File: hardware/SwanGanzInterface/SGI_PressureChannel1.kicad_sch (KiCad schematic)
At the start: 0 parts

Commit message: Developed amplifier circuits
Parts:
- added C10: 0.1u, Capacitor_SMD:C_0603_1608Metric, symbol Device:C
- added C11, C12: C, symbol Device:C
- added C13: 0.1u, symbol Device:C
- added R10, R11, R12: R, symbol Device:R
- added R13, R14: 0R, symbol Device:R
- added U4: INA122D, Package_SO:SOIC-8_5.3x5.3mm_P1.27mm, symbol SGI_SymbolLib:INA122D
- added U5: OPA2350, Package_DIP:DIP-8_W7.62mm, symbol SGI_SymbolLib:OPA2350PA
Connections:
- new net: R13.2, R14.1, U5.2 (-)
- new net: C11.1, R11.2, R12.1
- new net: C12.1, R12.2, U5.3 (+)
- new net: R10.1, U4.1 (RG+)
- new net: R11.1, U4.6 (OUT)
- new net: R10.2, U4.8 (RG-)
- new net +3V3A: C10.2, C13.1, U4.7 (+VS), U5.8 (V+)
- new net AGND: C10.1, C11.2, C13.2, R13.1, U4.4 (-VS), U4.5 (REF), U5.4 (V-)
- new net Pres1AmpOut: C12.2, R14.2, U5.1

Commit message: Filter Parameters
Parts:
- C11, C12: value C -> 0.1u
- R11, R12: value R -> 32k
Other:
- note added: "49.736 Hz Cutoff"
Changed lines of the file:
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@@
 	(generator "eeschema")
 	(generator_version "9.0")
-	(paper "A3")
+	(paper "A4")
 	(title_block
 		(title "Swan Ganz Interface")
-		(date "2025-12-20")
+		(date "2026-01-12")
 		(rev "Rev 1.0")
 		(company "Univerisity of Texas at Austin")
@@
 		(comment 2 "Ashton Knecht, Jack Son, Nathan DeLaRosa, Jerry Xia")
 		(comment 3 "Faculty Mentor - Dr. Valvano")
+	)
+	(text "49.736 Hz Cutoff"
+		(exclude_from_sim no)
+		(at 83.185 97.79 0)
+		(effects
+			(font
+				(size 2.54 2.54)
+			)
+		)
 	)
 	(junction
@@
 			)
 		)
-		(property "Value" "C"
+		(property "Value" "0.1u"
 			(at 105.41 71.755 0)
 			(effects
@@
 			)
 		)
-		(property "Value" "R"
+		(property "Value" "32k"
 			(at 111.76 62.23 90)
 			(effects
@@
 			)
 		)
-		(property "Value" "R"
+		(property "Value" "32k"
 			(at 97.79 62.23 90)
 			(effects
@@
 			)
 		)
-		(property "Value" "C"
-			(at 131.445 57.15 90)
-			(effects
-				(font
+		(property "Value" "0.1u"
+			(at 132.715 57.15 90)
+			(effects
+				(font

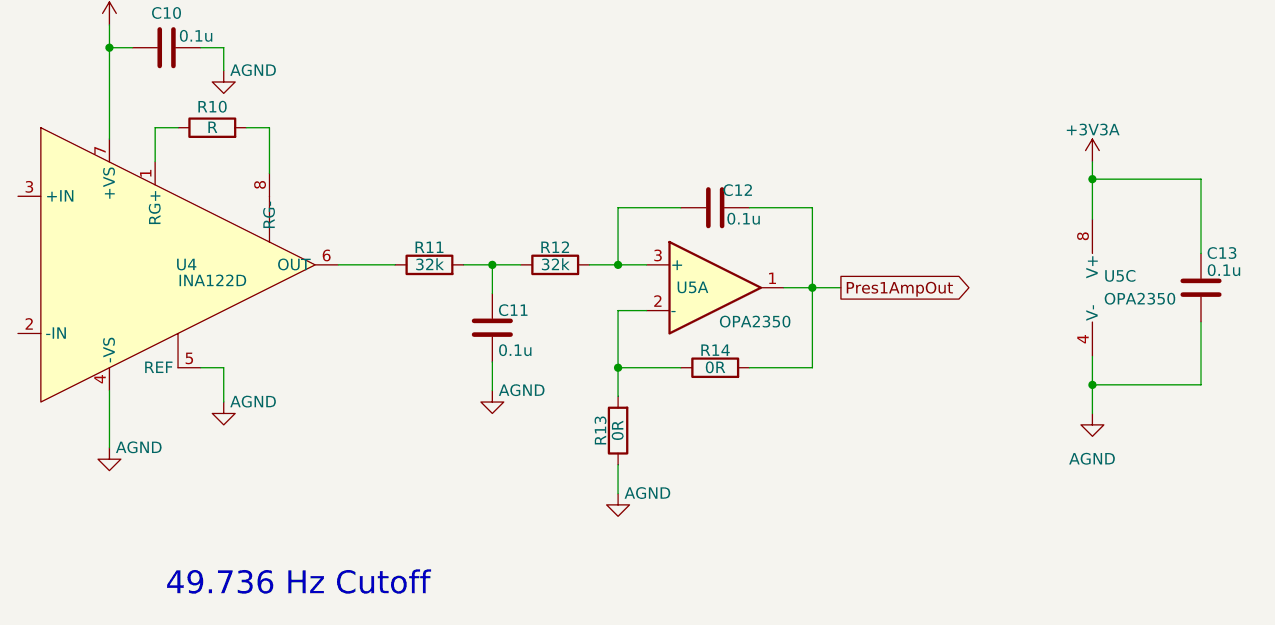
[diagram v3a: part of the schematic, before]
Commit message: Finished MSP-LP Symbol, Started Pressure_Connector Symbol
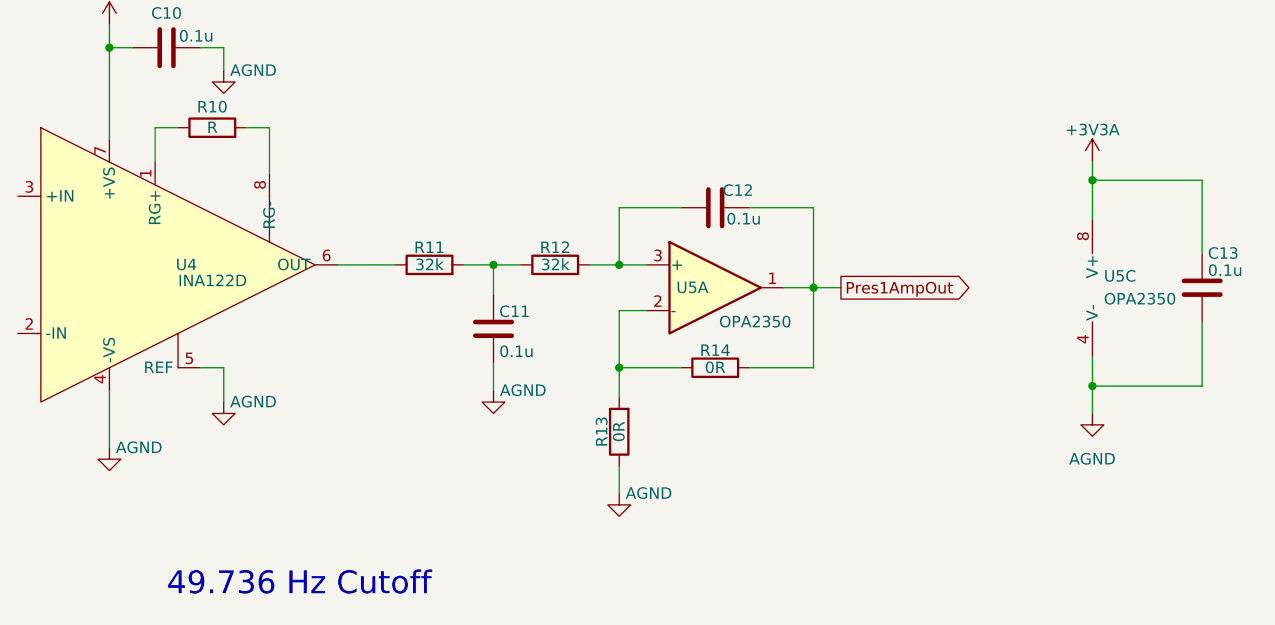
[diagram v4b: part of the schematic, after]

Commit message: Pressure Connector - Syncing for development
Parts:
- added U8: ~, symbol SGI_SymbolLib:Pressure_Connector
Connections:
- net AGND: now also U8.4 (VDD)
- net at U4.2 (-IN): now also U8.3 (SIG-)
- net at U4.3 (+IN): now also U8.2 (SIG+)
- new net P1_VCC: U8.1 (VCC)

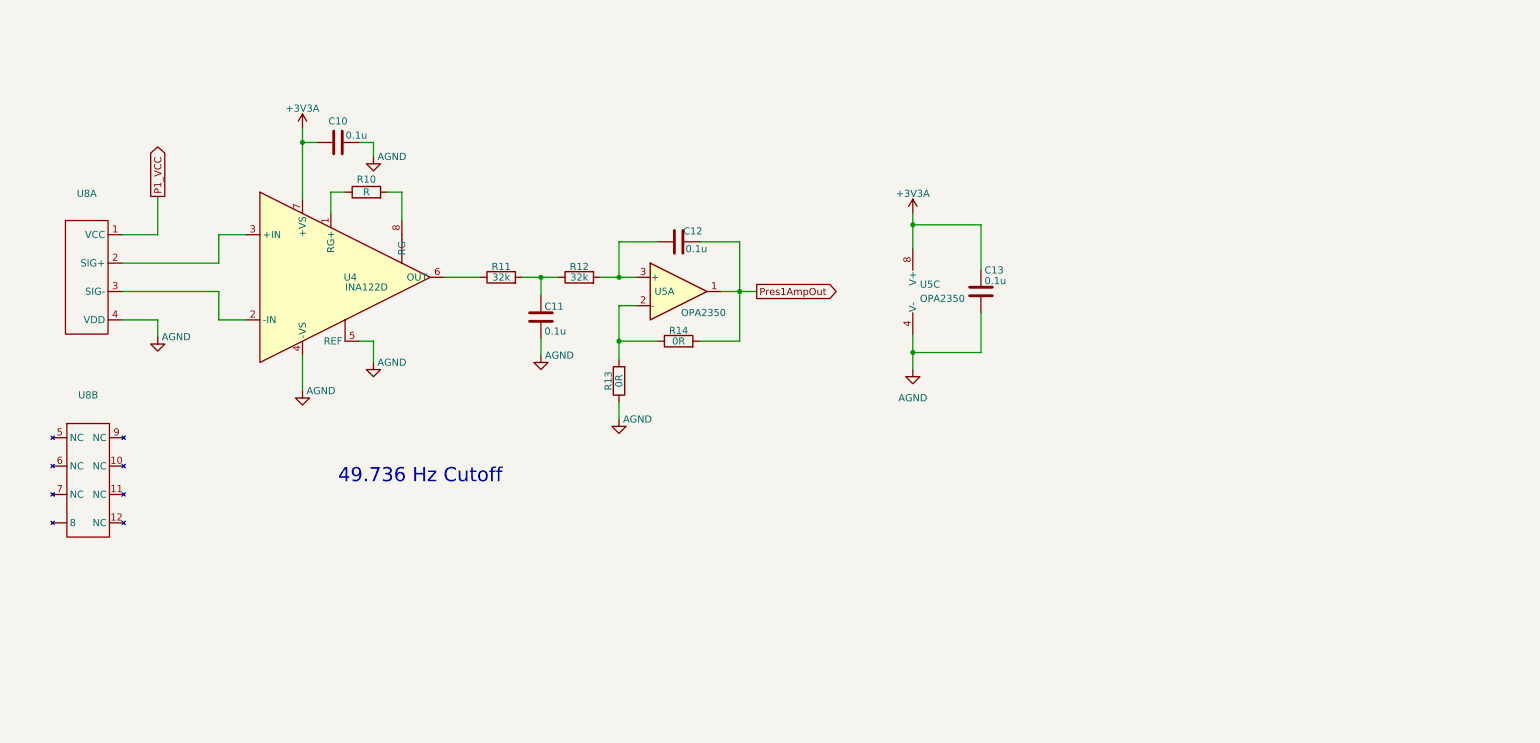
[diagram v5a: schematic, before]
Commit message: Updated gain and added power connector
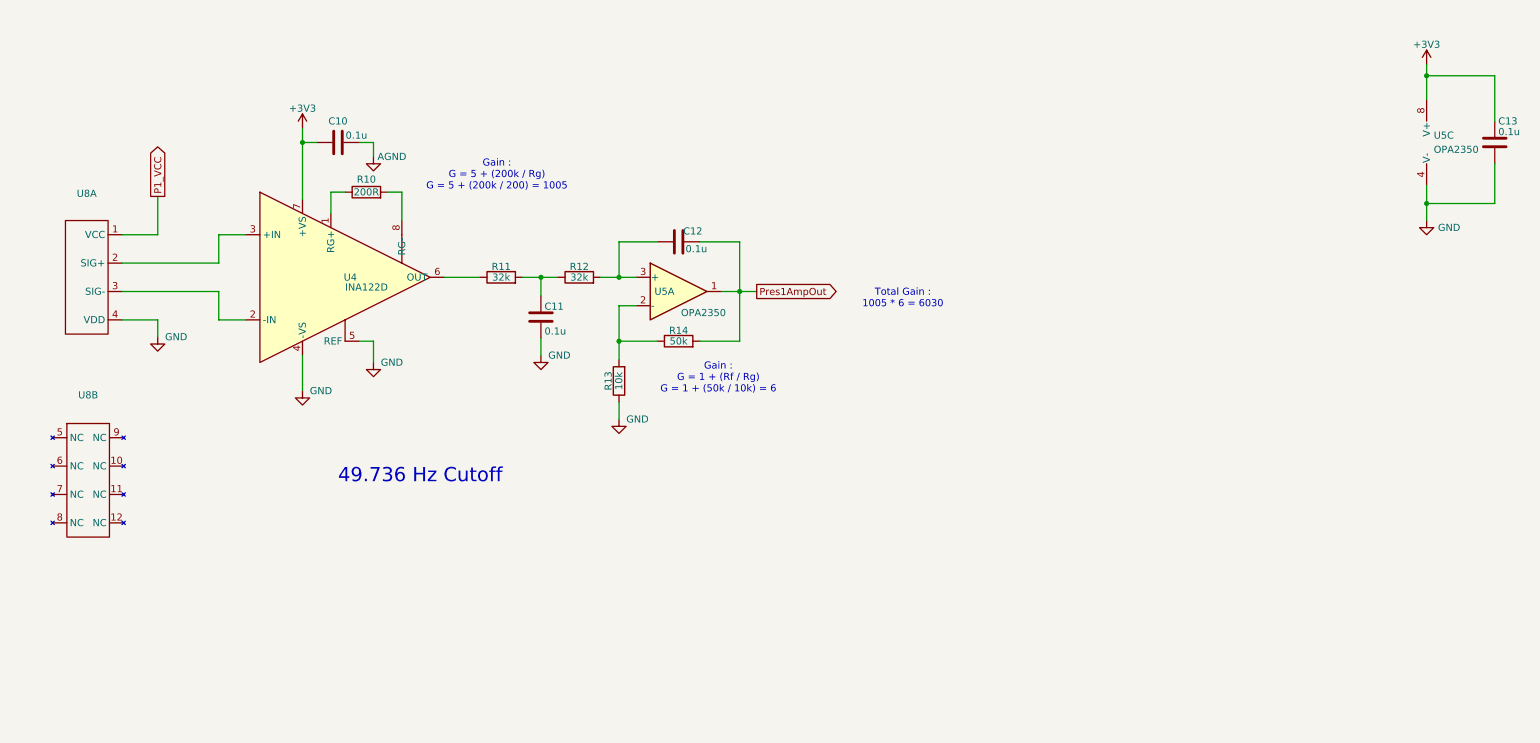
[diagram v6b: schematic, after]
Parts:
- R10: value R -> 200R
- R13: value 0R -> 10k
- R14: value 0R -> 50k
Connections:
- net AGND: no longer C11.2, C13.2, R13.1, U4.4 (-VS), U4.5 (REF), U5.4 (V-), U8.4 (VDD)
- net +3V3A renamed +3V3
- new net GND: C11.2, C13.2, R13.1, U4.4 (-VS), U4.5 (REF), U5.4 (V-), U8.4 (VDD)
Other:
- note added: "Gain : G = 1 + (Rf / Rg) G = 1 + (50k / 10k) = 6"
- note added: "Gain : G = 5 + (200k / Rg) G = 5 + (200k / 200) = 1005"
- note added: "Total Gain : 1005 * 6 = 6030"
- moved on the sheet: C13, U5C
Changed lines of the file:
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@@
 		(comment 3 "Faculty Mentor - Dr. Valvano")
+	)
+	(text "Total Gain :\n1005 * 6 = 6030"
+		(exclude_from_sim no)
+		(at 169.672 66.04 0)
+		(effects
+			(font
+				(size 1.27 1.27)
+			)
+		)
+	)
+	(text "Gain :\nG = 1 + (Rf / Rg)\nG = 1 + (50k / 10k) = 6"
+		(exclude_from_sim no)
+		(at 136.652 80.264 0)
+		(effects
+			(font
+				(size 1.27 1.27)
+			)
+		)
 	)
 	(text "49.736 Hz Cutoff"
@@
 		)
 	)
+	(text "Gain :\nG = 5 + (200k / Rg)\nG = 5 + (200k / 200) = 1005"
+		(exclude_from_sim no)
+		(at 97.028 43.942 0)
+		(effects
+			(font
+				(size 1.27 1.27)
+			)
+		)
+	)
 	(junction
 		(at 104.902 62.23)
@@
 	)
 	(junction
-		(at 171.45 75.692)
+		(at 263.398 49.022)
 		(diameter 0)
 		(color 0 0 0 0)
@@
 	)
 	(junction
-		(at 171.45 52.832)
+		(at 263.398 26.162)
 		(diameter 0)
 		(color 0 0 0 0)
@@
 	(wire
 		(pts
-			(xy 171.45 52.832) (xy 171.45 50.8)
+			(xy 263.398 26.162) (xy 263.398 24.13)
 		)
 		(stroke
@@
 	(wire
 		(pts
-			(xy 183.642 75.692) (xy 171.45 75.692)
+			(xy 275.59 49.022) (xy 263.398 49.022)
 		)
 		(stroke
@@
 	(wire
 		(pts
-			(xy 171.45 75.692) (xy 171.45 72.39)
+			(xy 263.398 49.022) (xy 263.398 45.72)
 		)
 		(stroke
@@
 	(wire
 		(pts
-			(xy 183.642 68.58) (xy 183.642 75.692)
+			(xy 275.59 41.91) (xy 275.59 49.022)
 		)
 		(stroke
@@
 	(wire
 		(pts
-			(xy 171.45 52.832) (xy 171.45 57.15)
+			(xy 263.398 26.162) (xy 263.398 30.48)
 		)
 		(stroke
@@
 	(wire
 		(pts
-			(xy 171.45 75.692) (xy 171.45 78.74)
+			(xy 263.398 49.022) (xy 263.398 52.07)
 		)
 		(stroke
@@
 	(wire
 		(pts
-			(xy 183.642 60.96) (xy 183.642 52.832)
+			(xy 275.59 34.29) (xy 275.59 26.162)
 		)
 		(stroke
@@
 	(wire
 		(pts
-			(xy 183.642 52.832) (xy 171.45 52.832)
+			(xy 275.59 26.162) (xy 263.398 26.162)
 		)
 		(stroke
@@
 			)
 		)
-		(property "Value" "0R"
+		(property "Value" "50k"
 			(at 129.54 73.66 90)
 			(effects
@@
 			)
 		)
-		(property "Value" "AGND"
+		(property "Value" "GND"
 			(at 108.204 76.2 0)
 			(effects
@@
 			)
 		)
-		(property "Value" "AGND"
+		(property "Value" "GND"
 			(at 65.532 82.55 0)
 			(effects
@@
 			)
 		)
-		(property "Value" "AGND"
+		(property "Value" "GND"
 			(at 122.174 87.63 0)
 			(effects
@@
 	(symbol
 		(lib_id "SGI_SymbolLib:OPA2350PA")
-		(at 173.99 64.77 0)
+		(at 265.938 38.1 0)
 		(unit 3)
 		(exclude_from_sim no)
@@
 		(fields_autoplaced yes)
 		(property "Reference" "U5"
-			(at 172.72 63.4999 0)
+			(at 264.668 36.8299 0)
 			(effects
 				(font
@@
 		)
 		(property "Value" "OPA2350"
-			(at 172.72 66.0399 0)
+			(at 264.668 39.3699 0)
 			(effects
 				(font
@@
 		)
 		(property "Footprint" "Package_DIP:DIP-8_W7.62mm"
-			(at 173.99 56.515 0)
+			(at 265.938 29.845 0)
 			(effects
 				(font
@@
 		)
 		(property "Datasheet" "kicad-embed://OPAx350.pdf"
-			(at 174.625 58.42 0)
+			(at 266.573 31.75 0)
 			(effects
 				(font
@@
 		)
 		(property "Description" "Precision, 38-MHz, Low-Noise, Low-Power, RRIO, CMOS Operational Amplifier, DIP-8"
-			(at 173.99 64.77 0)
+			(at 265.938 38.1 0)
 			(effects
 				(font
@@
 	(symbol
 		(lib_id "power:GNDA")
-		(at 171.45 78.74 0)
+		(at 263.398 52.07 0)
 		(unit 1)
 		(exclude_from_sim no)
@@
 		(fields_autoplaced yes)
 		(property "Reference" "#PWR028"
-			(at 171.45 85.09 0)
-			(effects
-				(font
-					(size 1.27 1.27)
-				)
-				(hide yes)
-			)
-		)
-		(property "Value" "AGND"
-			(at 171.45 83.82 0)
-			(effects
-				(font
-					(size 1.27 1.27)
-				)
+			(at 263.398 58.42 0)
+			(effects
+				(font
+					(size 1.27 1.27)
+				)
+				(hide yes)
+			)
+		)
+		(property "Value" "GND"
+			(at 265.43 53.3399 0)
+			(effects
+				(font
+					(size 1.27 1.27)
+				)
+				(justify left)
 			)
 		)
 		(property "Footprint" ""
-			(at 171.45 78.74 0)
+			(at 263.398 52.07 0)
 			(effects
 				(font
@@
 		)
 		(property "Datasheet" ""
-			(at 171.45 78.74 0)
+			(at 263.398 52.07 0)
 			(effects
 				(font
@@
 		)
 		(property "Description" "Power symbol creates a global label with name \"GNDA\" , analog ground"
-			(at 171.45 78.74 0)
+			(at 263.398 52.07 0)
 			(effects
 				(font
@@
 			)
 		)
-		(property "Value" "+3V3A"
+		(property "Value" "+3V3"
 			(at 62.23 32.004 0)
 			(effects
@@
 			)
 		)
-		(property "Value" "AGND"
+		(property "Value" "GND"
 			(at 39.624 72.898 0)
 			(effects
@@
 			)
 		)
-		(property "Value" "R"
+		(property "Value" "200R"
 			(at 73.66 46.99 90)
 			(effects
@@
 			)
 		)
-		(property "Value" "AGND"
+		(property "Value" "GND"
 			(at 78.232 77.47 0)
 			(effects
@@
 	(symbol
 		(lib_id "Device:C")
-		(at 183.642 64.77 0)
+		(at 275.59 38.1 0)
 		(unit 1)
 		(exclude_from_sim no)
@@
 		(dnp no)
 		(property "Reference" "C13"
-			(at 184.277 60.96 0)
+			(at 276.225 34.29 0)
 			(effects
 				(font
@@
 		)
 		(property "Value" "0.1u"
-			(at 184.277 62.865 0)
+			(at 276.225 36.195 0)
 			(effects
 				(font
@@
 		)
 		(property "Footprint" ""
-			(at 184.6072 68.58 0)
+			(at 276.5552 41.91 0)
 			(effects
 				(font
@@
 		)
 		(property "Datasheet" "~"
-			(at 183.642 64.77 0)
+			(at 275.59 38.1 0)
 			(effects
 				(font
@@
 		)
 		(property "Description" "Unpolarized capacitor"
-			(at 183.642 64.77 0)
+			(at 275.59 38.1 0)
 			(effects
 				(font
@@
 			)
 		)
-		(property "Value" "0R"
+		(property "Value" "10k"
 			(at 118.872 80.772 90)
 			(effects
@@
 		(pin "4"
 		)
-		(pin ""
+		(pin "8"
 		)
 		(pin "2"
@@
 	(symbol
 		(lib_id "power:+3V3")
-		(at 171.45 50.8 0)
+		(at 263.398 24.13 0)
 		(unit 1)
 		(exclude_from_sim no)
@@
 		(dnp no)
 		(property "Reference" "#PWR027"
-			(at 171.45 54.61 0)
-			(effects
-				(font
-					(size 1.27 1.27)
-				)
-				(hide yes)
-			)
-		)
-		(property "Value" "+3V3A"
-			(at 171.45 47.244 0)
+			(at 263.398 27.94 0)
+			(effects
+				(font
+					(size 1.27 1.27)
+				)
+				(hide yes)
+			)
+		)
+		(property "Value" "+3V3"
+			(at 263.398 20.574 0)
 			(effects
 				(font
@@
 		)
 		(property "Footprint" ""
-			(at 171.45 50.8 0)
+			(at 263.398 24.13 0)
 			(effects
 				(font
@@
 		)
 		(property "Datasheet" ""
-			(at 171.45 50.8 0)
+			(at 263.398 24.13 0)
 			(effects
 				(font
@@
 		)
 		(property "Description" "Power symbol creates a global label with name \"+3V3\""
-			(at 171.45 50.8 0)
+			(at 263.398 24.13 0)
 			(effects
 				(font
@@
 		(pin "4"
 		)
-		(pin ""
+		(pin "8"
 		)
 		(pin "2"

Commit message: Reverse Polarity Fet, Updated Notes, Added second gain stage for pressure, General Updates
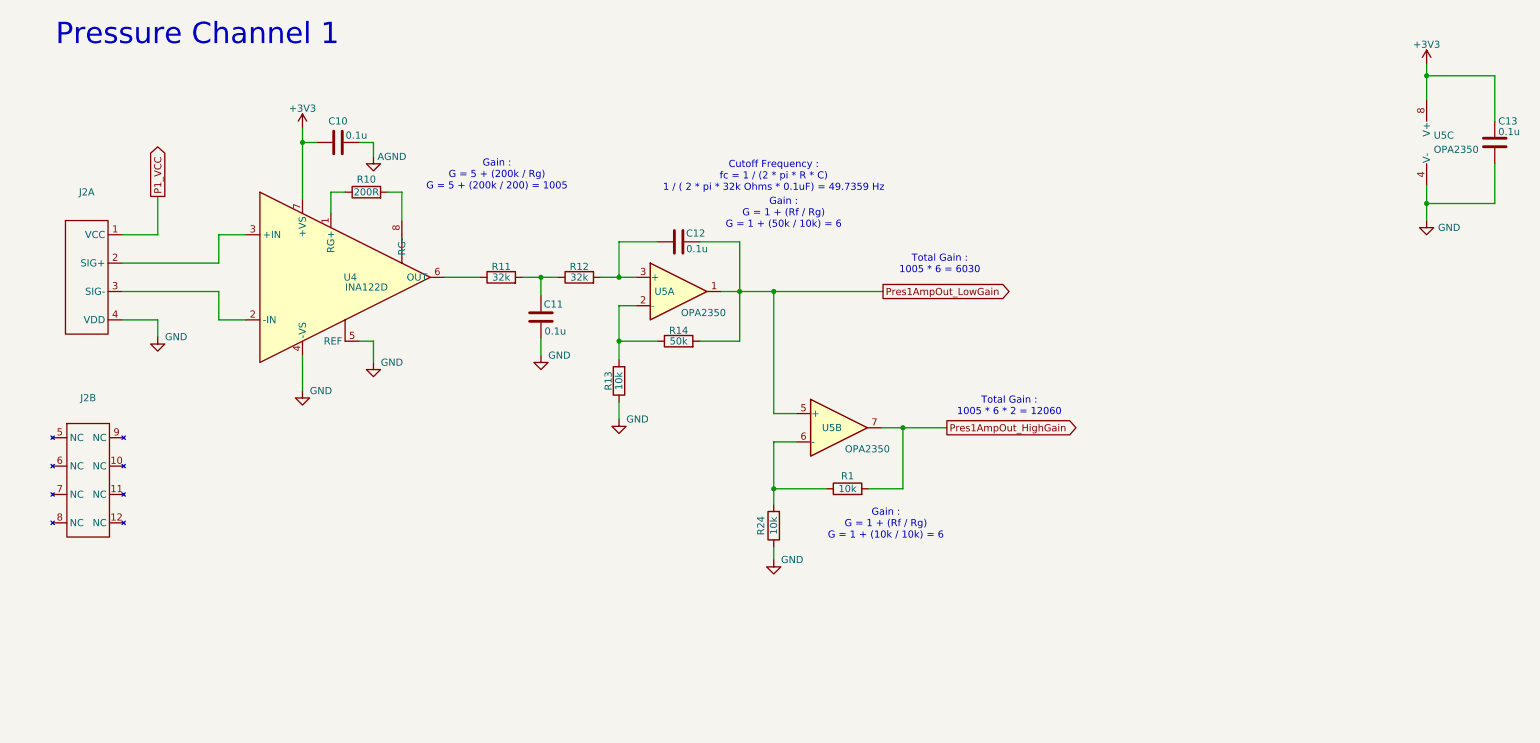
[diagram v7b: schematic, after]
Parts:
- added R1, R24: 10k, symbol Device:R
- added unit 2 of U5
- renumbered U8 to J2
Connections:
- net GND: now also R24.1
- net Pres1AmpOut renamed Pres1AmpOut_LowGain
- net Pres1AmpOut_LowGain: now also U5.5 (+)
- new net: R1.1, R24.2, U5.6 (-)
- new net Pres1AmpOut_HighGain: R1.2, U5.7
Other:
- note added: "Cutoff Frequency : fc = 1 / (2 * pi * R * C) 1 / ( 2 * pi * 32k Ohms * 0.1uF) = 49.7359 Hz"
- note added: "Gain : G = 1 + (Rf / Rg) G = 1 + (10k / 10k) = 6"
- note added: "Pressure Channel 1"
- note added: "Total Gain : 1005 * 6 * 2 = 12060"
- note removed: "49.736 Hz Cutoff"
